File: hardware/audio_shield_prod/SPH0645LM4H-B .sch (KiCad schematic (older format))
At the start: 6 parts

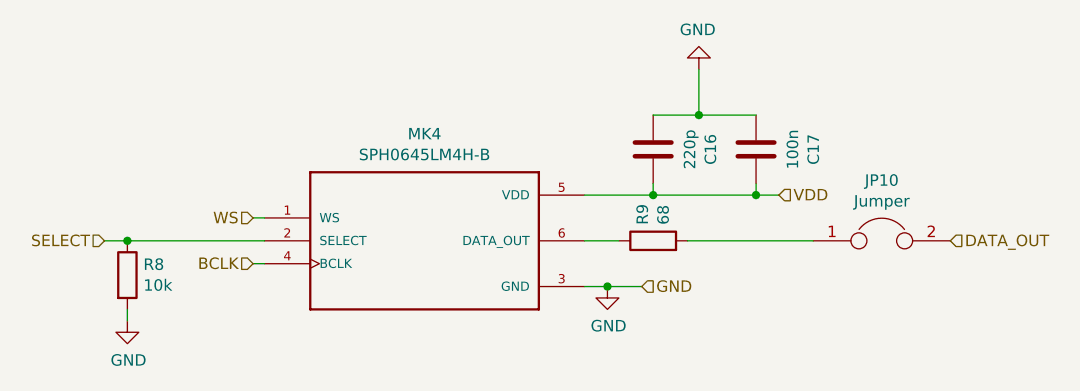
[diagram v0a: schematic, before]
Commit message: Edit component attribute for eurocircuit manufacturing
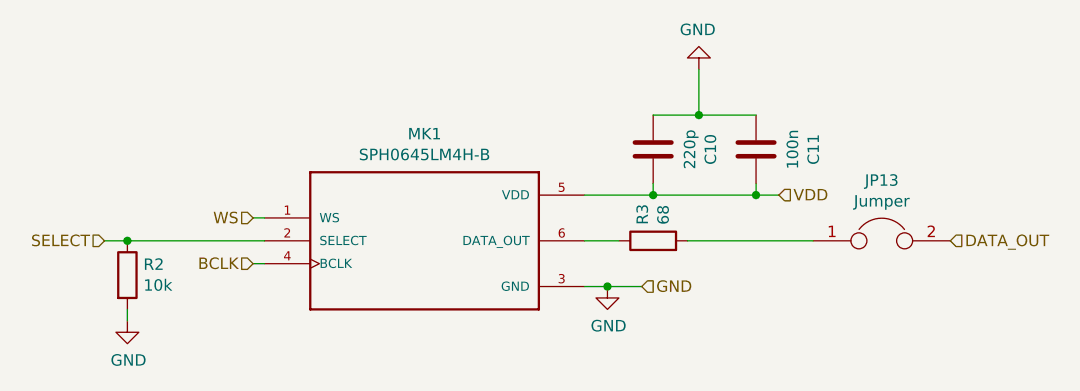
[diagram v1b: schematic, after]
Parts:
- JP12: Supplier (none) -> np
- R2, R3: Description (none) -> Thick film resistor 0.1W 1%
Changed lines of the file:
@@
 AR Path="/5F0910F0/5F09357C" Ref="MK7"  Part="1"
 AR Path="/5F0910F8/5F09357C" Ref="MK8"  Part="1"
-F 0 "MK4" H 5000 3667 50  0000 C CNN
+F 0 "MK1" H 5000 3667 50  0000 C CNN
 F 1 "SPH0645LM4H-B" H 5000 3576 50  0000 C CNN
 F 2 "audio_shield:MIC_SPH0645LM4H-B" H 5000 3200 50  0001 L BNN
@@
 AR Path="/5F0910F0/5F0947D1" Ref="R14"  Part="1"
 AR Path="/5F0910F8/5F0947D1" Ref="R16"  Part="1"
-F 0 "R8" H 3770 3396 50  0000 L CNN
+F 0 "R2" H 3770 3396 50  0000 L CNN
 F 1 "10k" H 3770 3305 50  0000 L CNN
 F 2 "Resistor_SMD:R_0603_1608Metric" V 3630 3350 50  0001 C CNN
@@
 F 5 "300-56-687" H 3700 3350 50  0001 C CNN "Supplier ref."
 F 6 "0.0084" H 3700 3350 50  0001 C CNN "Price"
+F 7 "Thick film resistor 0.1W 1%" H 3700 3350 50  0001 C CNN "Description"
 	1    3700 3350
 	1    0    0    -1
@@
 AR Path="/5F0910F0/5F09559C" Ref="C23"  Part="1"
 AR Path="/5F0910F8/5F09559C" Ref="C25"  Part="1"
-F 0 "C17" V 6702 2800 50  0000 C CNN
+F 0 "C11" V 6702 2800 50  0000 C CNN
 F 1 "100n" V 6611 2800 50  0000 C CNN
 F 2 "Capacitor_SMD:C_0603_1608Metric" H 6488 2650 50  0001 C CNN
@@
 AR Path="/5F0910F0/5F096212" Ref="C22"  Part="1"
 AR Path="/5F0910F8/5F096212" Ref="C24"  Part="1"
-F 0 "C16" V 6252 2800 50  0000 C CNN
+F 0 "C10" V 6252 2800 50  0000 C CNN
 F 1 "220p" V 6161 2800 50  0000 C CNN
 F 2 "Capacitor_SMD:C_0603_1608Metric" H 6038 2650 50  0001 C CNN
@@
 AR Path="/5F0910F0/5F0963B1" Ref="R15"  Part="1"
 AR Path="/5F0910F8/5F0963B1" Ref="R17"  Part="1"
-F 0 "R9" H 6070 3246 50  0000 L CNN
+F 0 "R3" H 6070 3246 50  0000 L CNN
 F 1 "68" H 6070 3155 50  0000 L CNN
 F 2 "Resistor_SMD:R_0603_1608Metric" V 5930 3200 50  0001 C CNN
@@
 F 5 "301-49-821" H 6000 3200 50  0001 C CNN "Supplier ref."
 F 6 " 0.0265" H 6000 3200 50  0001 C CNN "Price"
+F 7 "Thick film resistor 0.1W 1%" H 6000 3200 50  0001 C CNN "Description"
 	1    6000 3200
 	0    -1   -1   0
@@
 AR Path="/5F0950A2/5F1DEE78" Ref="JP11"  Part="1"
 AR Path="/5F04603F/5F1DEE78" Ref="JP13"  Part="1"
-F 0 "JP10" H 7000 3464 50  0000 C CNN
+F 0 "JP13" H 7000 3464 50  0000 C CNN
 F 1 "Jumper" H 7000 3373 50  0000 C CNN
 F 2 "Jumper:SolderJumper-2_P1.3mm_Bridged_Pad1.0x1.5mm" H 7000 3200 50  0001 C CNN
 F 3 "~" H 7000 3200 50  0001 C CNN
+F 4 "np" H 7000 3200 50  0001 C CNN "Supplier"
 	1    7000 3200
 	1    0    0    -1
